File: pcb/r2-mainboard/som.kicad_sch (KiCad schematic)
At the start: 11 parts, among them J21 MICRO_SD(TFC-WPAPR-08), X2 PCM-071

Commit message: R2: the six approved edits, and one of them was already done
Owner-approved 2026-08-19, KiCad closed for the pass.

1. R225 22k -> 20.5K/1%, LCSC C57105 (0402WGF2052TCE, UNI-ROYAL, the
   family the rest of the board already uses). Rendered and checked:
   R224 390k over R225 20.5k with R213 100k injecting VGH_DAC, so
   20.5||100 = 17.01k and VGH = 1.2 x (1 + 390/17.01) = 28.71 V at
   DAC = 0 -- exactly epd-port.md 10.3's target.
2. The five sense-divider caps that carried codes for the wrong
   capacitance -> C1523 (0402B102K500NT, 1 nF 50 V X7R, JLC Basic,
   5.3 M stock). One part covers both the 25 V and 50 V positions.
2b. R88/R224 -> C54920667 (HRC0402F3903DNTO, 390k 1%, 20 k stock).
   C25782 had 14 units against two per board. The owner found this one;
   both obvious alternatives were traps -- C23150 is 0603, and C44937
   is 3.9 ohm despite "390K" in its part number.
3. C147 set DNP rather than deleted. panel.md 7 had already ruled that
   J6.7/J6.44 stay; that covered the pins but not the capacitor on the
   dead net. DNP drops it from placement, keeps the topology of a frozen
   sheet untouched, and leaves the footprint if a future panel drives
   the rail. in_bom stays yes -- that is this board's convention for all
   13 DNP parts, so they show up flagged rather than vanishing.
4. Ten duplicate #PWR references renumbered to #PWR1112-1121 on the
   battery sheet, which was the colliding side in every case.
5. J3 was already deleted on 2026-08-15. No work needed.
6. Specter -> Reflow across 22 files: 14 sheets, 7 generators, the
   project file. .history/ deliberately untouched.

Verified as one change: netlist before and after has 518 nets with
identical pin membership, and epd_power and epd were rendered to PNG and
inspected.

Docs updated to match: epd-port.md 10 is applied rather than designed,
frontlight.md 1 loses the "9 in series is inferred" hedge (the vendor
listing confirms 2 x 9), and io-expansion.md 4's "only guess on this
sheet" is resolved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
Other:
- title: Glider-R2 / Specter mainboard -> Glider-R2 / Reflow mainboard
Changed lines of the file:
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@@
 	(paper "A3")
 	(title_block
-		(title "Glider-R2 / Specter mainboard")
+		(title "Glider-R2 / Reflow mainboard")
 		(date "2026-08-15")
 		(rev "A")

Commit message: R2: the SoM can now reset the MCU and force its bootloader (WP8 closed)
tools/patch_som_mcu_recovery.py applies mcu.md 5.8. On som, A59 and A60
lose their no-connects and gain SOM_MCU_NRST / SOM_MCU_BOOT0. On mcu,
three parts land on empty canvas at x>300:

  Q9    AO3400A  Transistor_FET:Q_NMOS_GSD, SOT-23, C347475
  R510  100k     gate pull-down
  R511  1k       series into PA14

NRST goes through the FET rather than straight to the pin, because the
MCU gates the SoM's own supply -- "SoM off, MCU alive" is the normal
standby state, and a direct tie would let an unpowered A59 clamp
MCU_NRST toward a dead VDDSHV_CANUART and hold the MCU in reset for
good. With Q9 the default is safe in every combination: gate low or SoM
unpowered leaves NRST to the STM32's internal pull-up.

BOOT0 needs no FET -- nothing on R2 drives PA14 high, so R40's pull-down
already defines the safe state, and R511 doubles as the contention limit
against an ST-LINK on the shared SWCLK pin.

Verified: 518 nets before and after; the only membership changes are
MCU_NRST += Q9.3, MCU_SWCLK += R511.2, GND += Q9.2/R510.2, plus the two
new nets and the two unconnected- entries that went away. Rendered to
PNG and inspected twice -- the first layout ran the MCU_NRST label
vertically into the BOOT0 row, so the drain now turns right first.

One trap recorded in mcu.md 5.8: set_sheet_pins re-lays every pin on a
root box, and the root's stubs and labels are positional, so adding two
pins silently rotated the membership of eighteen nets on the first run.
wire_root.py must be re-run after any sheet-pin change; the patch script
now does that itself and asserts on its exit code.

RM0444 (now in datasheets/) settles the factory question from source:
3.3.1 p.67, the EMPTY flag "allows easy programming of virgin devices by
the boot loader", so a blank board needs only an SD card. Riders: the
first flash needs a power cycle or OBL_LAUNCH to reload option bytes,
and the BOOT0 pin still earns its keep for recovery, w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
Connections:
- net SOM_MCU_NRST: now reaches X2.A59 (X_MCU_MCAN1_TX)
- net SOM_MCU_BOOT0: now reaches X2.A60 (X_MCU_MCAN1_RX)
- no-connect marks 147 -> 145
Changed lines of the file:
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@@
 	)
 	(no_connect
-		(at 177.8 76.2)
-	)
-	(no_connect
 		(at 386.08 199.39)
 	)
@@
 	)
 	(no_connect
-		(at 177.8 73.66)
-	)
-	(no_connect
 		(at 177.8 116.84)
 	)
@@
 		)
 	)
+	(wire
+		(pts
+			(xy 177.8 73.66) (xy 154.94 73.66)
+		)
+		(stroke
+			(width 0)
+			(type default)
+		)
+	)
+	(hierarchical_label "SOM_MCU_NRST"
+		(shape bidirectional)
+		(at 154.94 73.66 180)
+		(effects
+			(font
+				(size 1.27 1.27)
+			)
+			(justify right)
+		)
+	)
+	(wire
+		(pts
+			(xy 177.8 76.2) (xy 154.94 76.2)
+		)
+		(stroke
+			(width 0)
+			(type default)
+		)
+	)
+	(hierarchical_label "SOM_MCU_BOOT0"
+		(shape bidirectional)
+		(at 154.94 76.2 180)
+		(effects
+			(font
+				(size 1.27 1.27)
+			)
+			(justify right)
+		)
+	)

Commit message: R2: two interrupts that could never fire, and the SoM footprint
The EXTI collisions mcu.md §3.4 found are applied. An EXTI line is picked
by the pin's *number*, so TOUCH_INT# on PC3 was fighting PD3 GAUGE_ALRT#
and PEN_INT# on PC6 was fighting PD6 QON_SNS -- as drawn neither touch nor
pen could raise an interrupt at all. Each swaps with an output, which needs
no line, so it costs nothing. FL_INT# gets PB12 at the same time, which was
frontlight.md §10.3's own first suggestion; §9's later push for PB7 was
wrong, because PC7 KEY_PREV# holds EXTI7.

518 -> 517 nets, the drop being the PB12 unconnected- pseudo-net, and
exactly five membership changes. Every hierarchical label in the project
now has a counterpart -- DANGLING_OK is empty and ERC excluding
footprint_link_issues is 32, down from 105.

The PCM-071 footprint is built rather than downloaded, because two drawings
have landed that over-determine it: Samtec's own vector land pattern (parsed
from the content stream, every measurement agreeing with a printed dimension
to under 1 um) and L-1038e.A5 Figure 7, which is a carrier-board drawing.
The trap it contains is that the alignment hole is NOT on the connector's
centreline -- it is 1.054 mm from one row and 5.118 from the other, and
Figure 7 dimensions the holes, so assuming a centred hole puts both
connectors 2.06 mm out. The check worth trusting is the one nothing forces:
the B and C rows land 0.982 and 0.998 mm inside the module's edges.

Also: U41's speed grade is settled -2 -- LCSC has no -3 in FTG256 at all,
and caster.xise's -3 is ISE's untouched default (valueState="default"), not
a choice anyone made. But -2's MCB is rated 667 Mb/s against the 666.67 this
design runs, so fpga.md §1.1 asks for one free ISE build before the order.

And a bring-up landmine: epd_pos_rails_good() accepts VGH <= 28.0 V while
R2's own R225 change puts it at 28.41 V nominal. A correctly built board
would fatal() at every EPD power-up. epd-port.md §10.5.

Co-Authored-By: Claude Op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
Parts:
- X2: footprint footprints:PCM-071_2xBTH-060-01-L-D-A-K -> r2:PCM-071_2xBTH-060-01-L-D-A-K
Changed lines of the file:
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@@
 			)
 		)
-		(property "Footprint" "footprints:PCM-071_2xBTH-060-01-L-D-A-K"
+		(property "Footprint" "r2:PCM-071_2xBTH-060-01-L-D-A-K"
 			(at 76.2 100.33 0)
 			(hide yes)
@@
 			)
 		)
-		(property "Footprint" "footprints:PCM-071_2xBTH-060-01-L-D-A-K"
+		(property "Footprint" "r2:PCM-071_2xBTH-060-01-L-D-A-K"
 			(at 213.36 88.9 0)
 			(hide yes)
@@
 			)
 		)
-		(property "Footprint" "footprints:PCM-071_2xBTH-060-01-L-D-A-K"
+		(property "Footprint" "r2:PCM-071_2xBTH-060-01-L-D-A-K"
 			(at 350.52 139.7 0)
 			(hide yes)

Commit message: R2: rebuild the SoM footprint on PHYTEC's DXF, and a BOM line nobody had
The 3D archive came with PCM-071_1573-1.dxf, which is vector and numeric
where L-1038e.A5 Figure 7 is a raster picture, and which PHYTEC's own
README names authoritative alongside the datasheets. It gives the four
60-pad columns, the pitch, the module outline and both M2.5 positions
directly.

It agreed with the picture-derived footprint to 8 um in x and 61 um in y.
61 um is 20 % of a 0.305 mm pad's width, so it is corrected: the pads now
sit exactly where the DXF puts them and the generator asserts it. The row
skew is 0.0 um -- the DXF's connector centrelines are 4.800 and 27.200,
symmetric about the module's midline, which nothing in Samtec's drawing
forces.

One contradiction had to be resolved rather than averaged. The DXF has four
1.100 mm holes 35.126 apart, which is neither Samtec's -A diameter nor its
"A" dimension, 4.7 mm from where Figure 7 puts the alignment holes. They are
the BSH plug's own locating holes: the -A option pegs each connector into
the board it is soldered to, so the plug's pegs land in the module and the
receptacle's land in ours, and the two sets never meet. Trusting them would
have put both connectors 0.62 mm out.

Building it turned up the gap that matters more: X2 is one symbol for the
MODULE, so the BOM has no line for the two BTH-060-01-L-D-A-K-TR the
assembler actually solders. LCSC C3646540, two per board, 60 in stock --
30 boards, now the tightest line on the BOM. som.md section 10.

Also closes D-7 and the SoM side from the owner: the sketch's "TTL
Interface" block is where the panel flex lands after folding under the
display, not a second PCB, so J6 gains a fixed orientation as well as a
fixed position; touch is the same. The SoM goes on the face away from the
panel. Nothing blocks Stage D any more.

The bulk 3D (49 MB of STEP/x_t) is gitignored -- the zip is committed, so
it is all recoverable; the DXF is committed extracted because the generator
parses it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
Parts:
- X2: BOM Comments (none) -> Plug-in module, bought from PHYTEC and fitted after assembl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; MPN (none) -> PCM-071; Manufacturer (none) -> PHYTEC
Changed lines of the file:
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@@
 	(wire
 		(pts
+			(xy 177.8 76.2) (xy 154.94 76.2)
+		)
+		(stroke
+			(width 0)
+			(type default)
+		)
+	)
+	(wire
+		(pts
 			(xy 104.14 130.81) (xy 114.3 130.81)
 		)
@@
 	(wire
 		(pts
+			(xy 177.8 73.66) (xy 154.94 73.66)
+		)
+		(stroke
+			(width 0)
+			(type default)
+		)
+	)
+	(wire
+		(pts
 			(xy 43.18 175.26) (xy 43.18 173.99)
 		)
@@
 		)
 	)
+	(hierarchical_label "SOM_MCU_NRST"
+		(shape bidirectional)
+		(at 154.94 73.66 180)
+		(effects
+			(font
+				(size 1.27 1.27)
+			)
+			(justify right)
+		)
+	)
 	(hierarchical_label "SOM_WAKE#"
 		(shape bidirectional)
@@
 		)
 	)
+	(hierarchical_label "SOM_MCU_BOOT0"
+		(shape bidirectional)
+		(at 154.94 76.2 180)
+		(effects
+			(font
+				(size 1.27 1.27)
+			)
+			(justify right)
+		)
+	)
 	(symbol
 		(lib_id "power:GND")
@@
 		(dnp no)
 		(property "Reference" "X2"
-			(at 45.72 11.43 0)
+			(at 56.642 36.83 0)
 			(show_name no)
 			(do_not_autoplace no)
@@
 		)
 		(property "Value" "PCM-071"
-			(at 45.72 13.97 0)
+			(at 56.642 39.37 0)
 			(show_name no)
 			(do_not_autoplace no)
@@
 			)
 		)
+		(property "MPN" "PCM-071"
+			(at 76.2 102.87 0)
+			(hide yes)
+			(show_name no)
+			(do_not_autoplace no)
+			(effects
+				(font
+					(size 1.27 1.27)
+				)
+			)
+		)
+		(property "Manufacturer" "PHYTEC"
+			(at 76.2 105.41 0)
+			(hide yes)
+			(show_name no)
+			(do_not_autoplace no)
+			(effects
+				(font
+					(size 1.27 1.27)
+				)
+			)
+		)
+		(property "BOM Comments" "Plug-in module, bought from PHYTEC and fitted after assembly -- NOT placed by the PCBA house. The parts that ARE soldered to this footprint are 2x Samtec BTH-060-01-L-D-A-K-TR, LCSC C3646540, and they are a separate purchase line this symbol does not generate. See som.md section 10."
+			(at 76.2 107.95 0)
+			(hide yes)
+			(show_name no)
+			(do_not_autoplace no)
+			(effects
+				(font
+					(size 1.27 1.27)
+				)
+			)
+		)
 		(property "Datasheet" ""
 			(at 76.2 100.33 0)
@@
 		)
 	)
-	(wire
-		(pts
-			(xy 177.8 73.66) (xy 154.94 73.66)
-		)
-		(stroke
-			(width 0)
-			(type default)
-		)
-	)
-	(hierarchical_label "SOM_MCU_NRST"
-		(shape bidirectional)
-		(at 154.94 73.66 180)
-		(effects
-			(font
-				(size 1.27 1.27)
-			)
-			(justify right)
-		)
-	)
-	(wire
-		(pts
-			(xy 177.8 76.2) (xy 154.94 76.2)
-		)
-		(stroke
-			(width 0)
-			(type default)
-		)
-	)
-	(hierarchical_label "SOM_MCU_BOOT0"
-		(shape bidirectional)
-		(at 154.94 76.2 180)
-		(effects
-			(font
-				(size 1.27 1.27)
-			)
-			(justify right)
-		)
-	)

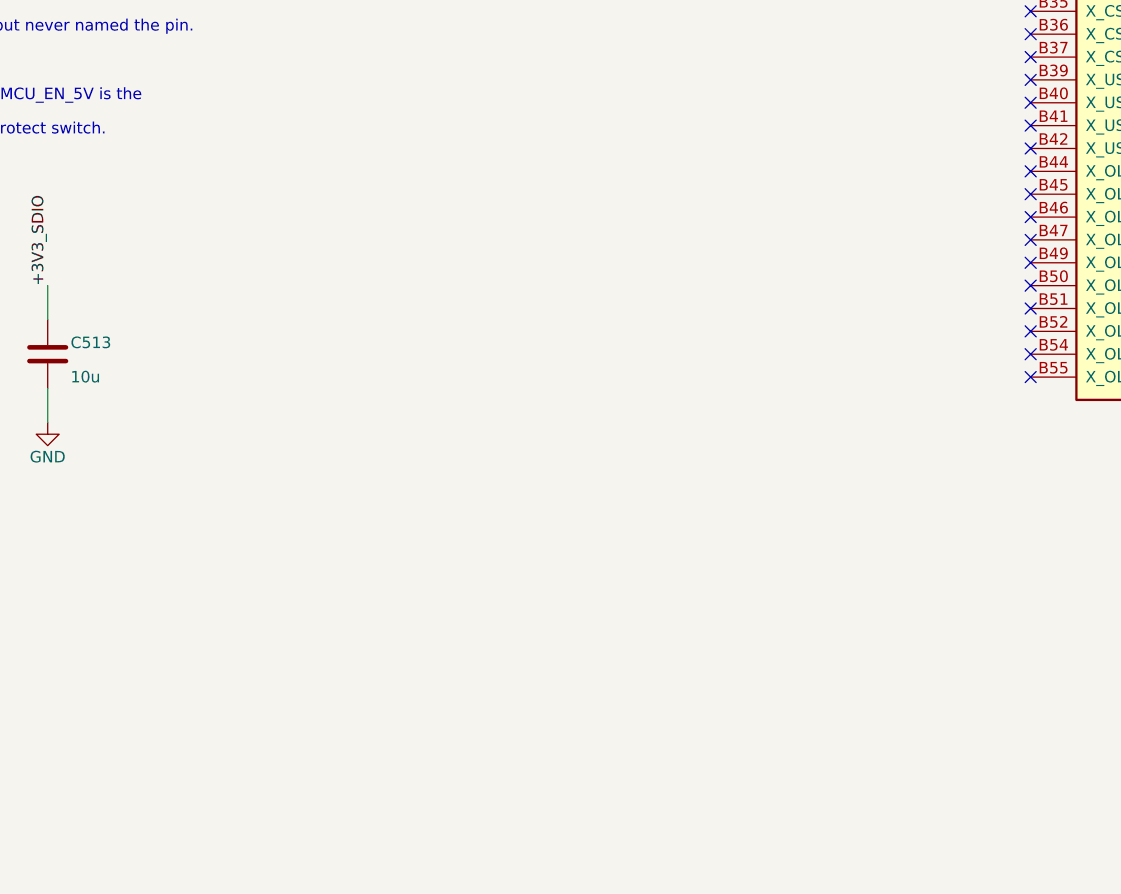
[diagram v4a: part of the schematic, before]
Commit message: R2: why there is no connector symbol, and the BOM line that was missing
The question was a good one and the answer is that the schematic models the
thing you reason about -- the SoM and its 240 signals -- while the footprint
models the thing you solder, two connectors at a fixed offset. That split is
deliberate (gen_som_symbol.py argued it) and PHYTEC's DXF has since made the
cost of the alternative concrete: the two connectors are staggered 4.800 mm
as well as spaced 22.400 mm, which is exactly the relationship a person
nudges by accident. As one footprint it cannot be got wrong.

The second reason is worse for the alternative. Samtec numbers its pads
1-120 alternating between rows; the module's pinout is A1-A60 / B1-B60 /
C1-C60 / D1-D60. "Just use the vendor part" is a 240-line renumbering on a
component where every pin is invisible to ERC.

Its only real cost was the missing BOM line, and that is now covered without
compromising the symbol: J26/J27 (the receptacles) and MK20 (the M2.5
hardware PHYTEC specifies) are purchase-only symbols on `r2:BOM_ITEM`, a
pin-less rectangle placed on_board=no. 517 nets before and after, none of
them in the netlist's components, ERC unchanged at 32. A grouped BOM export
now carries "J26,J27" as one line of quantity 2.

Samtec's own KiCad footprint arrived with the download and is an independent
check that passed: pad size, row spacing, pitch, span, hole diameter and the
2.032 hole offset all agree exactly. Notably Samtec's own file uses 0.500
pitch and 29.500 span rather than the 0.5001/29.507 in their dimension
table -- the same choice this generator made and the same numbers the DXF
gives. Adopted from it: the 1.991 hole offset, and solder_mask_margin 0.102,
which makes each row one gang opening with no webs. Correct at this pitch,
and better stated than inherited.

One trap recorded: the first placement landed on top of J21, because
scanning a sheet's (at ...) values finds symbol origins, not extents.

Co-Authored-By: Claude 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
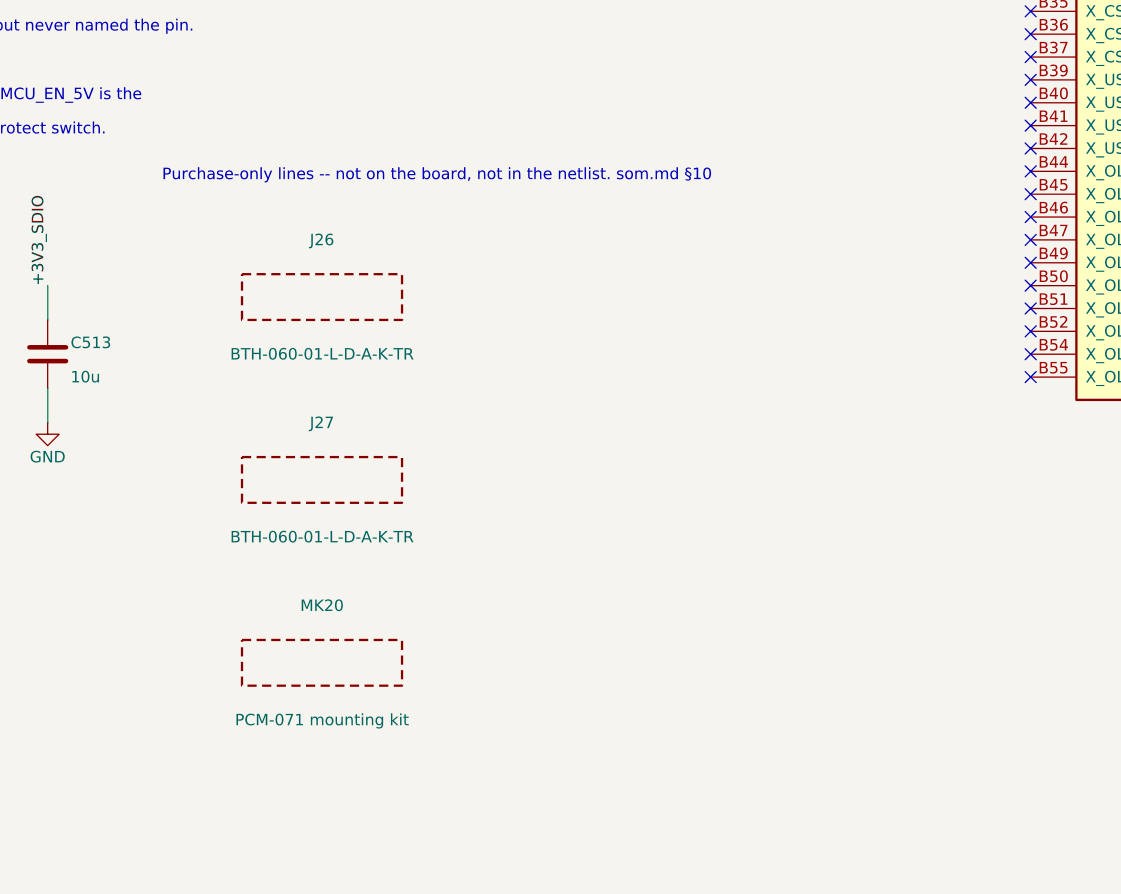
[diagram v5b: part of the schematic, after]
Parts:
- added J26, J27: BTH-060-01-L-D-A-K-TR, symbol r2:BOM_ITEM
- added MK20: PCM-071 mounting kit, symbol r2:BOM_ITEM
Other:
- note added: "Purchase-only lines -- not on the board, not in the netlist. som.md §10"
